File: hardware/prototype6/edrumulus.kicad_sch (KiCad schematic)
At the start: 97 parts, among them J1 Hi-Hat, J2 Snare, J3 Crash, J4 Ride, J5 Tom1, J6 Tom2, J7 Tom3, J8 Kick, J9 Hi-Hat-Ctrl, U1 ESP32-DEVKIT-V1, U3 MCP1754S-3302xMB

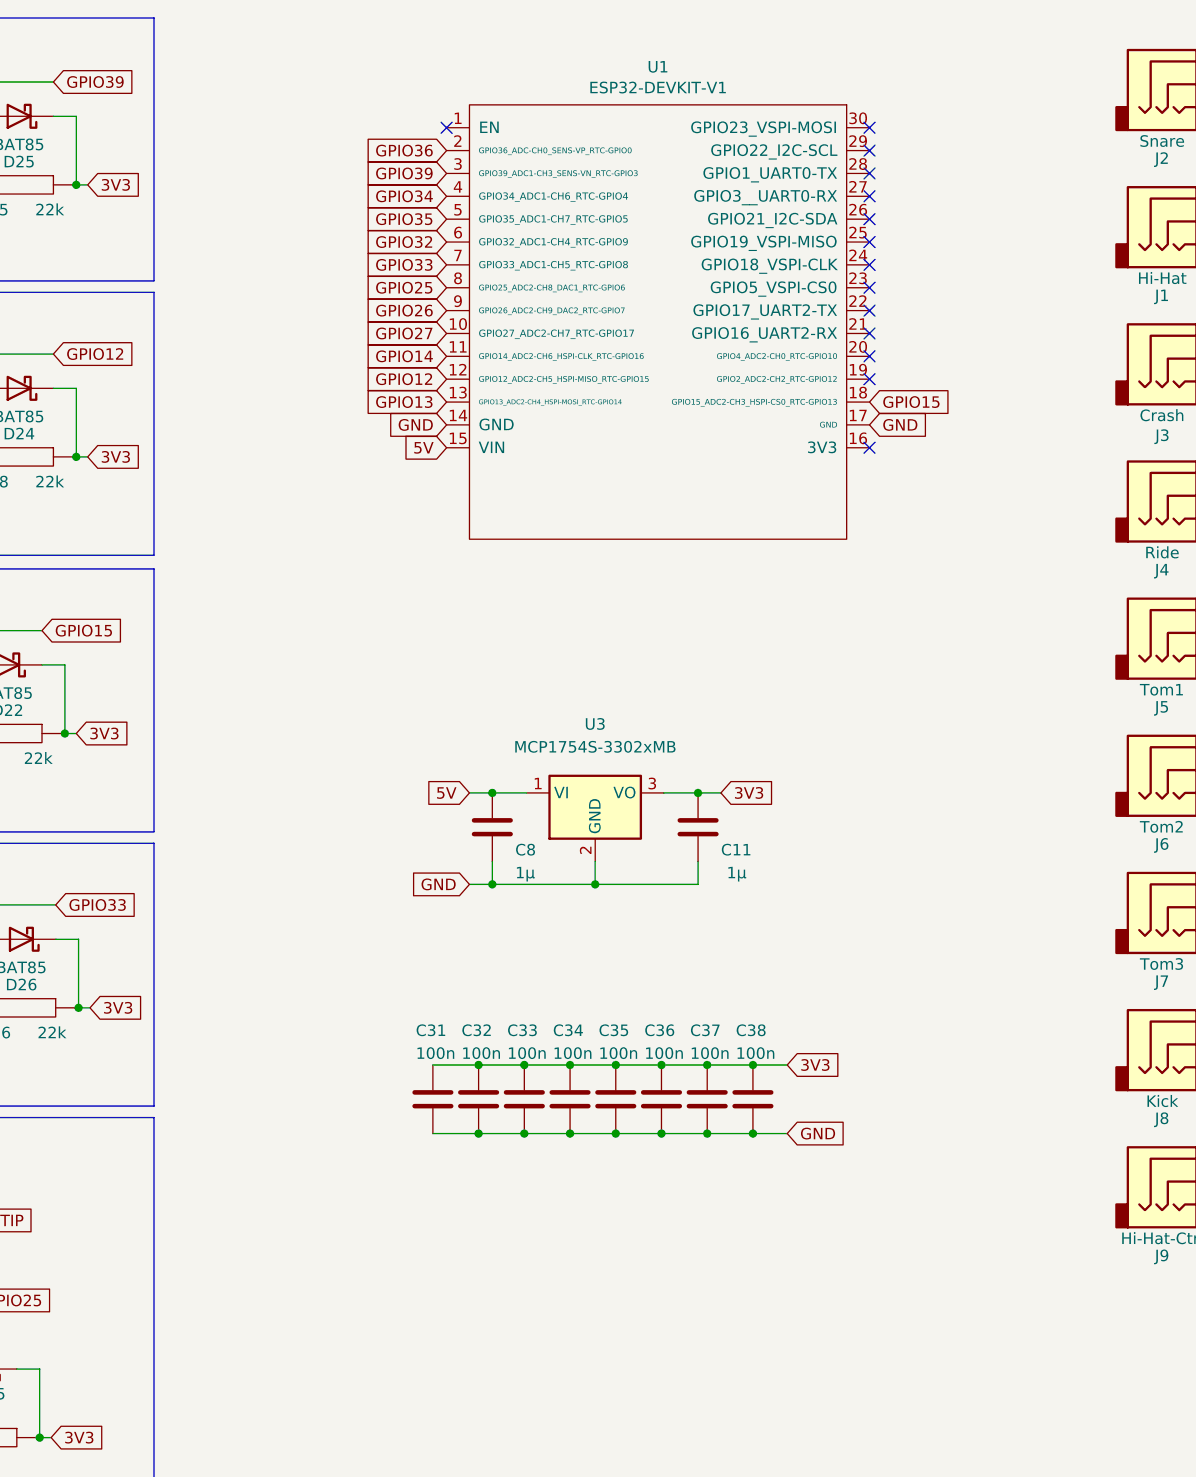
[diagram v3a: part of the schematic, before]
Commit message: added MIDI in/out for prototpye 6
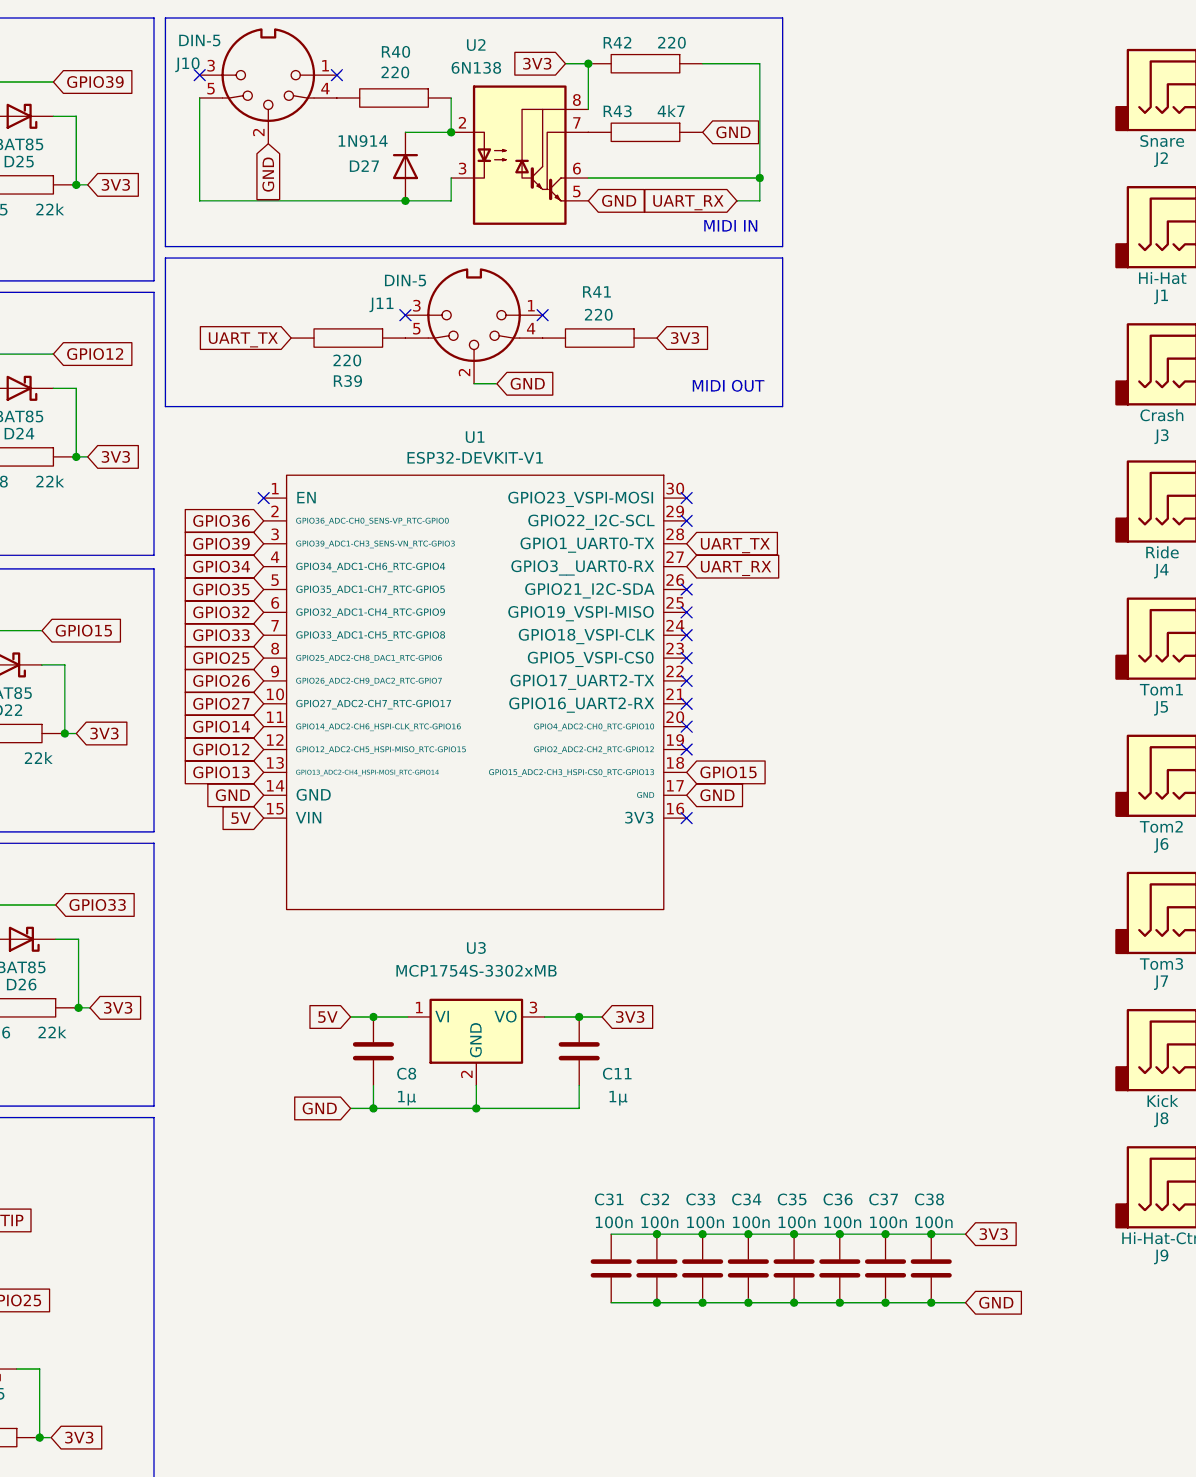
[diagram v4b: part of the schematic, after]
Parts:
- added D27: 1N914, Diode_THT:D_DO-35_SOD27_P7.62mm_Horizontal, symbol Diode:1N914
- added J10, J11: DIN-5, symbol Connector:DIN-5_180degree
- added R39, R40, R41, R42: 220, Resistor_THT:R_Axial_DIN0207_L6.3mm_D2.5mm_P10.16mm_Horizontal, symbol pspice:R
- added R43: 4k7, Resistor_THT:R_Axial_DIN0207_L6.3mm_D2.5mm_P10.16mm_Horizontal, symbol pspice:R
- added U2: 6N138, Package_DIP:DIP-8_W7.62mm_Socket, symbol Isolator:6N138
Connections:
- net 3V3: now also R41.1, R42.2, U2.8 (VCC)
- net GND: now also J10.2, J11.2, R43.1, U2.5 (GND)
- net UART_RX: now reaches U1.27 (GPIO3__UART0-RX)
- net UART_RX: now also R42.1, U2.6 (VO2)
- net UART_TX: now reaches U1.28 (GPIO1_UART0-TX)
- net UART_TX: now also R39.2
- new net: J11.4, R41.2
- new net: J11.5, R39.1
- new net: D27.1 (K), R40.1, U2.2 (C1)
- new net: D27.2 (A), J10.5, U2.3 (C2)
- new net: R43.2, U2.7 (VO1)
- new net: J10.4, R40.2
- no-connect marks 19 -> 21
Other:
- note added: "MIDI IN"
- note added: "MIDI OUT"
- moved on the sheet: C11, C31, C32, C33, C34, C35, C36, C37, C38, C8, U1, U3

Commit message: added footprint
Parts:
- C1, C10, C12, C13, C14, C2, C3, C4, C5, C6, C7, C9: footprint Capacitor_SMD:C_0603_1608Metric_Pad1.08x0.95mm_HandSolder -> (none)
- J10, J11: footprint (none) -> Connectors_UNITRA:DIN-5
- R1, R10, R11, R12, R13, R14, R15, R16, R17, R18, R19, R2, R20, R21, R22, R23, R24, R25, R26, R27, R28, R29, R3, R30, R31, R32, R33, R34, R35, R36, R37, R38, R4, R5, R6, R7, R8, R9: footprint (none) -> Resistor_THT:R_Axial_DIN0207_L6.3mm_D2.5mm_P10.16mm_Horizontal

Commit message: added initial PCB for prototype 6
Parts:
- C1, C10, C12, C13, C14, C2, C3, C31, C32, C33, C34, C35, C36, C37, C38, C4, C5, C6, C7, C9: footprint (none) -> Capacitor_THT:C_Disc_D5.0mm_W2.5mm_P5.00mm
- C11, C8: footprint (none) -> Capacitor_THT:CP_Radial_D8.0mm_P3.50mm

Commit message: more work on prototype 6
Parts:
- J10: value DIN-5 -> MIDI-IN
- J11: value DIN-5 -> MIDI-OUT
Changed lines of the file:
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@@
     (in_bom yes) (on_board yes)
     (property "Reference" "J11" (id 0) (at 157.988 50.8 0))
-    (property "Value" "DIN-5" (id 1) (at 160.528 48.26 0))
+    (property "Value" "MIDI-OUT" (id 1) (at 160.528 48.26 0))
     (property "Footprint" "Connectors_UNITRA:DIN-5" (id 2) (at 168.148 52.07 0)
       (effects (font (size 1.27 1.27)) hide)
@@
     (in_bom yes) (on_board yes)
     (property "Reference" "J10" (id 0) (at 136.398 24.13 0))
-    (property "Value" "DIN-5" (id 1) (at 137.668 21.59 0))
+    (property "Value" "MIDI-IN" (id 1) (at 137.668 21.59 0))
     (property "Footprint" "Connectors_UNITRA:DIN-5" (id 2) (at 145.288 25.4 0)
       (effects (font (size 1.27 1.27)) hide)
@@
     )
     (path "/5eb66693-ab1b-4459-a77e-81bcb06ca4d6"
-      (reference "J10") (unit 1) (value "DIN-5") (footprint "Connectors_UNITRA:DIN-5")
+      (reference "J10") (unit 1) (value "MIDI-IN") (footprint "Connectors_UNITRA:DIN-5")
     )
     (path "/03a8b23a-c991-47a6-b608-48bb34767196"
-      (reference "J11") (unit 1) (value "DIN-5") (footprint "Connectors_UNITRA:DIN-5")
+      (reference "J11") (unit 1) (value "MIDI-OUT") (footprint "Connectors_UNITRA:DIN-5")
     )
     (path "/add90365-59e6-451f-89f8-8665d94a32ba"

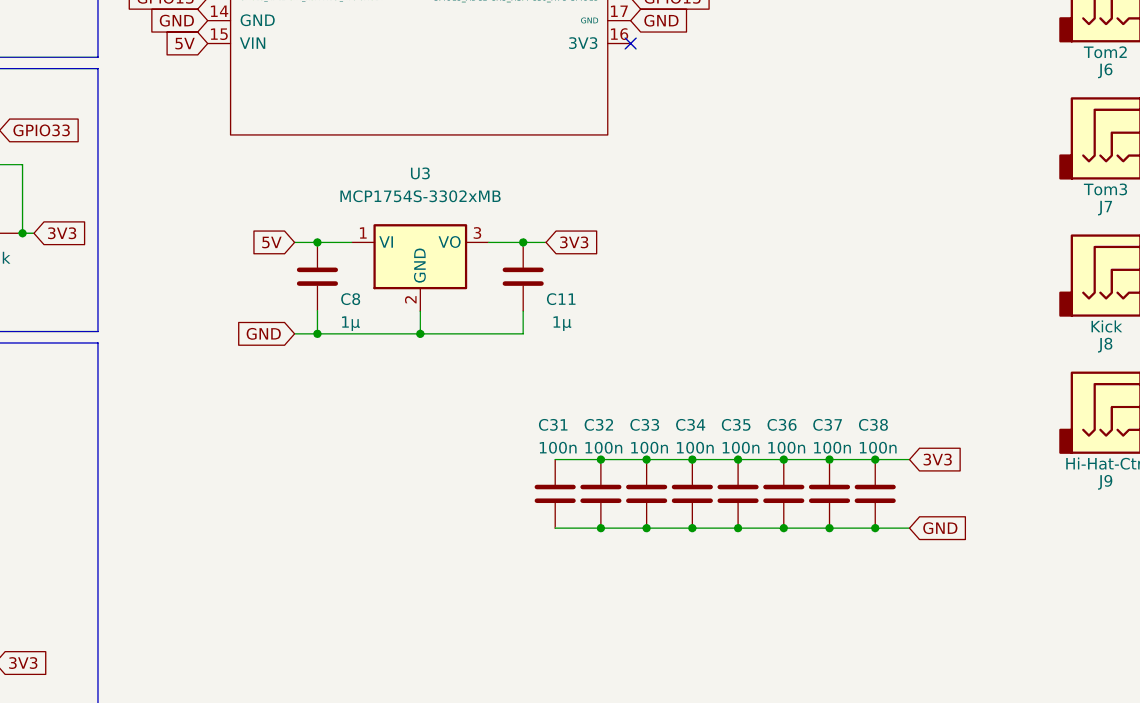
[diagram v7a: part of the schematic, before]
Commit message: use different regulator for prototype 6
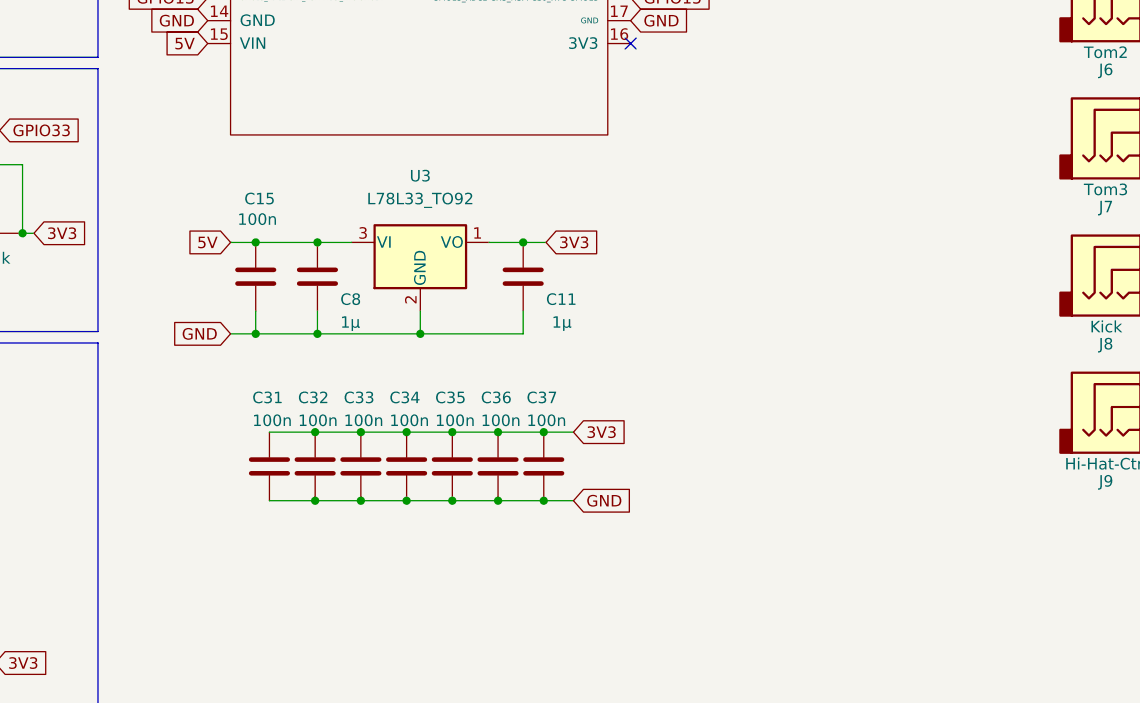
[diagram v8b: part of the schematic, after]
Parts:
- removed C38: 100n, Capacitor_THT:C_Disc_D5.0mm_W2.5mm_P5.00mm, symbol Device:C
- removed U3: MCP1754S-3302xMB, Package_TO_SOT_SMD:SOT-89-3, symbol Regulator_Linear:MCP1754S-3302xMB
- added C15: 100n, Capacitor_THT:C_Disc_D5.0mm_W2.5mm_P5.00mm, symbol Device:C
- added U3: L78L33_TO92, Package_TO_SOT_THT:TO-92_Inline, symbol Regulator_Linear:L78L33_TO92
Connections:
- net 3V3: now also U3.1 (VO)
- net 5V: now also C15.1, U3.3 (VI)
- net GND: now also C15.2, U3.2 (GND)
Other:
- moved on the sheet: C31, C32, C33, C34, C35, C36, C37
